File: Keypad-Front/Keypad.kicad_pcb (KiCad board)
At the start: 4 copper layers, 100.1 x 192.1 mm, 62 parts, among them J1 RTC STEMMA QT, J3 JST-PH 6, J4 JST-PH 6, J6 EXP QWIIC, J7 TOUCH QWIIC, U1 DS3231MZ, U2 LM1117-3.3, U3 CAP1214

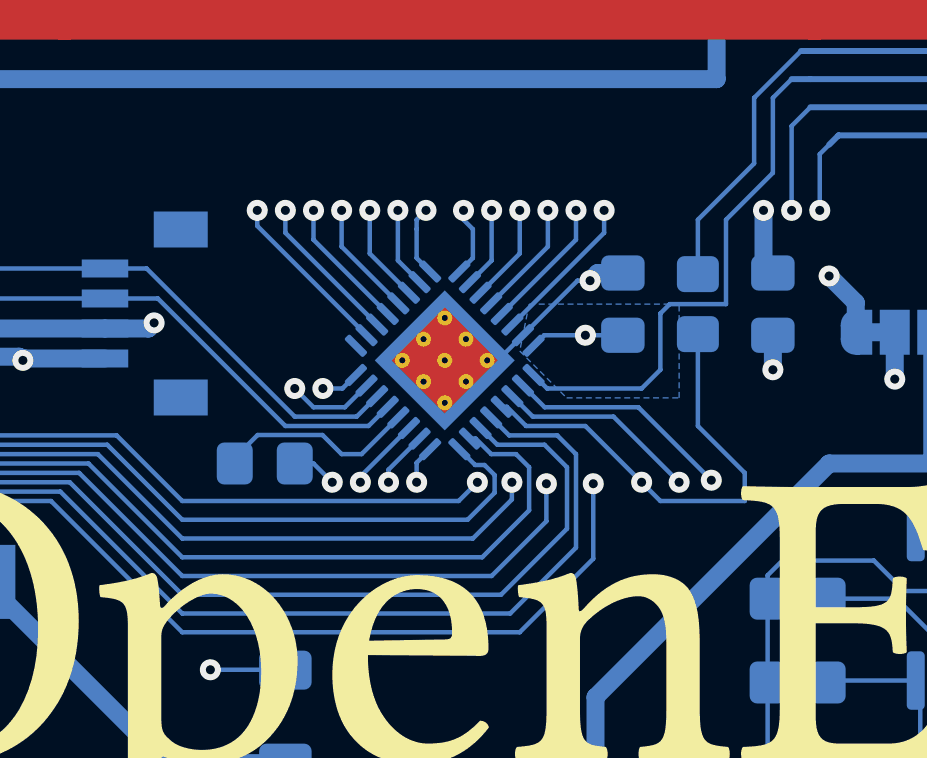
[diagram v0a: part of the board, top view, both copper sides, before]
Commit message: Fix schematic and PCB
1. Swap LED6 and LED11 so that the dual LED is on the high-power port.
   (This change isn't green-wired on the existing boards.)
2. Add 47pF series cap to TOUCH_GUARD to bring it into spec.
   (Measured at 80pF; CAP1214 supports 50pF max.)
3. Fix RESET -- it should be grounded, not tied high.
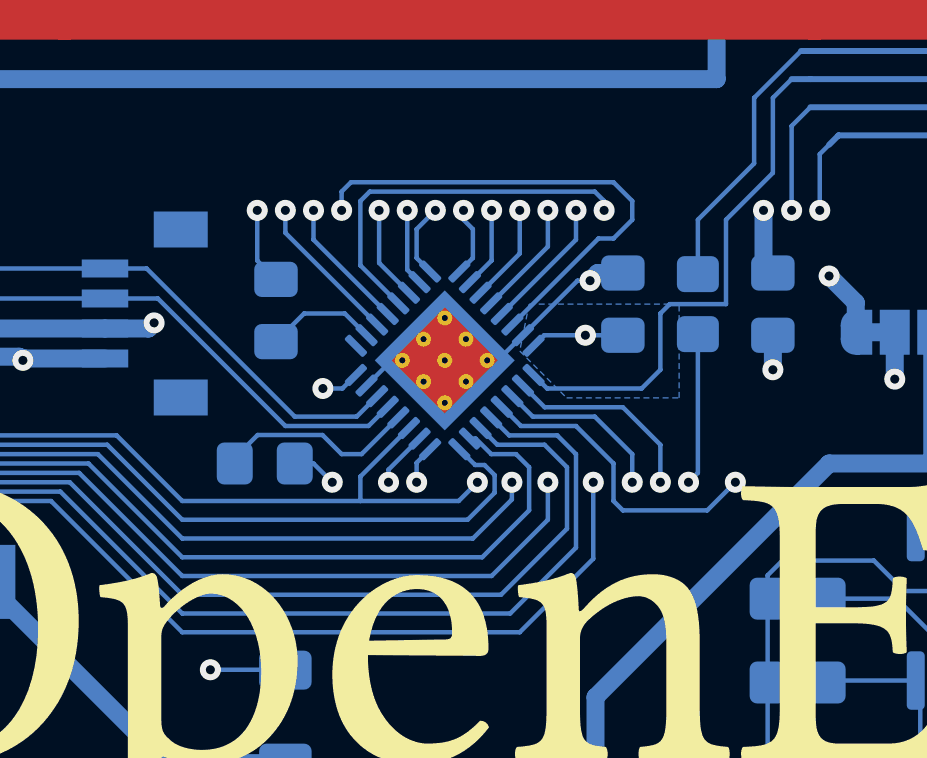
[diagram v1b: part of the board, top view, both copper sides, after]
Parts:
- added C5: 47pF, Capacitor_SMD:C_0805_2012Metric_Pad1.18x1.45mm_HandSolder, B.Cu at (102.5, 185.2)
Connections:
- U3 pad 12: /LED10 -> /LED6
- U3 pad 19: /LED6 -> /LED10
- U3 pad 23: +3.3V -> GND1
- U3 pad 26: /TOUCH_GUARD -> Net-(U3-CS1)
- U3 pad 29: /TOUCH_10 -> /TOUCH_6
- U3 pad 6: /TOUCH_6 -> /TOUCH_10
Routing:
- net /TOUCH_10: track 35.9 -> 48.8 mm
- net /TOUCH_5: track 77.5 -> 69.7 mm
- net /TOUCH_6: track 102.8 -> 110.3 mm
- net /LED10: track 89.2 -> 83.2 mm
- net /TOUCH_1: track 107.8 -> 101.9 mm
- net /LED6: track 134.4 -> 129.6 mm
- net +3.3V: track 58.3 -> 54.3 mm, vias 6 -> 5
- net /LED7: track 112.3 -> 108.6 mm
- net Net-(U3-CS1): track 0.00 -> 3.71 mm
- net /TOUCH_8: track 50.4 -> 46.8 mm
- net /LED4: track 144.2 -> 140.6 mm
- net /LED3: track 157.8 -> 161.2 mm
- net /TOUCH_GUARD: track 41.6 -> 38.5 mm
- net GND1: track 2021.0 -> 2022.5 mm

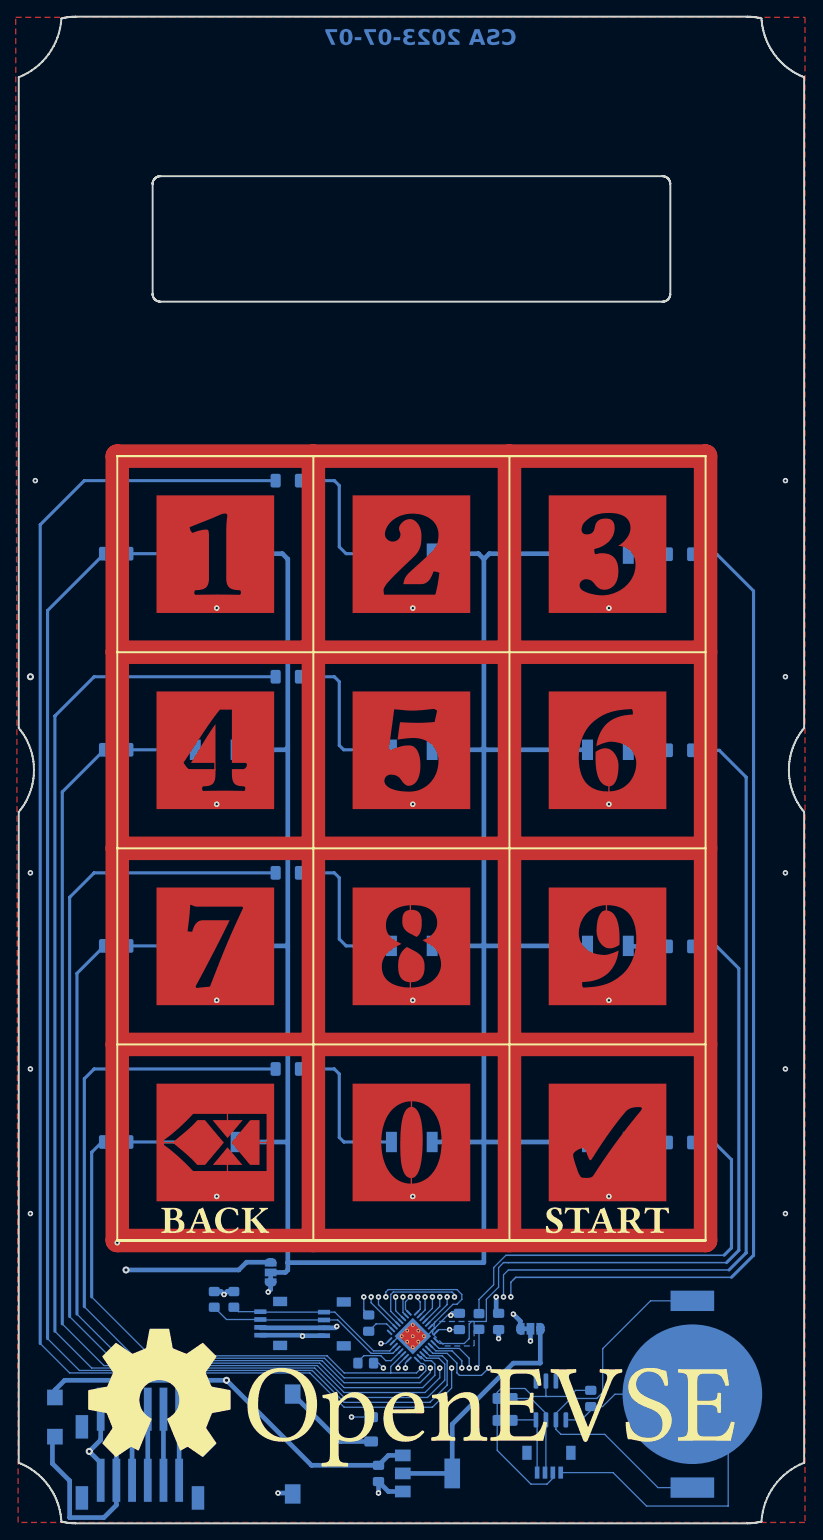
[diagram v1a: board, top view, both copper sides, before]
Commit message: Fix some errors in original boards; add RFID functionality
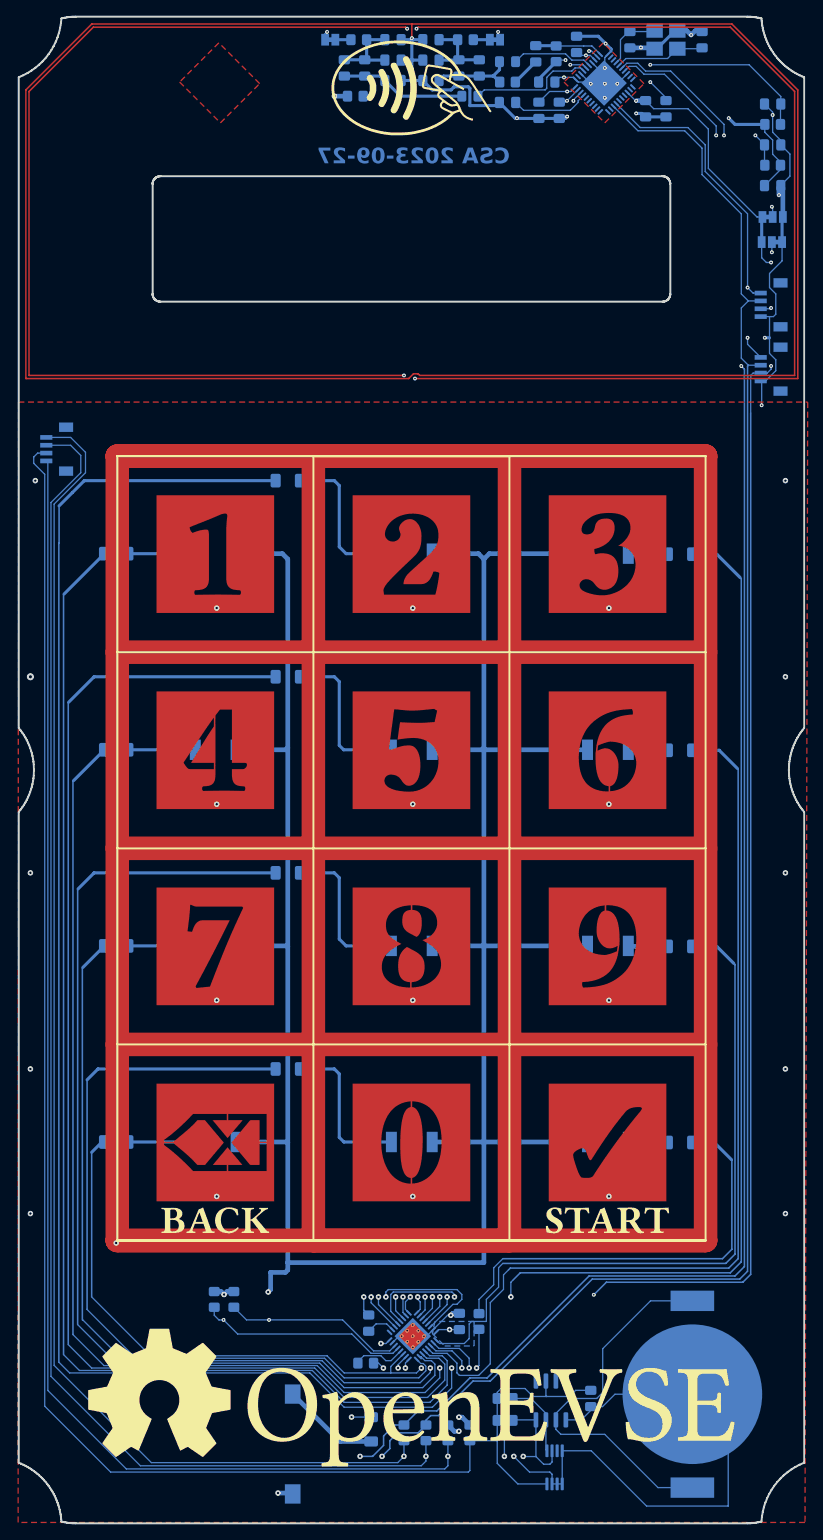
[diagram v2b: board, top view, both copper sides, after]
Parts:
- removed J3, J4: JST-PH 6, Keypad:JST-PH-6-SMD
- removed TP13: 5V, TestPoint:TestPoint_Pad_2.0x2.0mm
- removed TP14: Guard, Keypad:Touch_Pad_D1.0mm
- removed TP15: 12V, TestPoint:TestPoint_Pad_2.0x2.0mm
- removed U2: LM1117-3.3, Package_TO_SOT_SMD:SOT-223-3_TabPin2
- added C10: 10uF, Capacitor_SMD:C_0805_2012Metric_Pad1.18x1.45mm_HandSolder, B.Cu at (154.0, 29.8)
- added C11: .1uF, Capacitor_SMD:C_0805_2012Metric_Pad1.18x1.45mm_HandSolder, B.Cu at (129.0, 22.2)
- added C12: N/C, Capacitor_SMD:C_0805_2012Metric_Pad1.18x1.45mm_HandSolder, B.Cu at (99.4, 25.2)
- added C13: .1uF, Capacitor_SMD:C_0805_2012Metric_Pad1.18x1.45mm_HandSolder, B.Cu at (154.0, 40.2)
- added C14: 10uF, Capacitor_SMD:C_0805_2012Metric_Pad1.18x1.45mm_HandSolder, B.Cu at (154.0, 35.0)
- added C15: .1uF, Capacitor_SMD:C_0805_2012Metric_Pad1.18x1.45mm_HandSolder, B.Cu at (140.4, 30.4)
- added C16: 220pF, Capacitor_SMD:C_0805_2012Metric_Pad1.18x1.45mm_HandSolder, B.Cu at (105.6, 26.8)
- added C17: 220pF, Capacitor_SMD:C_0805_2012Metric_Pad1.18x1.45mm_HandSolder, B.Cu at (110.4, 26.8)
- added C18: N/C, Capacitor_SMD:C_0805_2012Metric_Pad1.18x1.45mm_HandSolder, B.Cu at (116.6, 25.2)
- added C19: 22pF, Capacitor_SMD:C_0805_2012Metric_Pad1.18x1.45mm_HandSolder, B.Cu at (102.0, 25.2)
- added C20: 22pF, Capacitor_SMD:C_0805_2012Metric_Pad1.18x1.45mm_HandSolder, B.Cu at (114.0, 25.2)
- added C21: 100pF, Capacitor_SMD:C_0805_2012Metric_Pad1.18x1.45mm_HandSolder, B.Cu at (105.6, 24.2)
- added C22: 100pF, Capacitor_SMD:C_0805_2012Metric_Pad1.18x1.45mm_HandSolder, B.Cu at (110.4, 24.2)
- added C23: N/C, Capacitor_SMD:C_0805_2012Metric_Pad1.18x1.45mm_HandSolder, B.Cu at (105.6, 21.6)
- added C24: N/C, Capacitor_SMD:C_0805_2012Metric_Pad1.18x1.45mm_HandSolder, B.Cu at (110.4, 21.6)
- added C25: 1000pF, Capacitor_SMD:C_0805_2012Metric_Pad1.18x1.45mm_HandSolder, B.Cu at (123.8, 23.4)
- added C26: .1uF, Capacitor_SMD:C_0805_2012Metric_Pad1.18x1.45mm_HandSolder, B.Cu at (125.2, 27.0)
- added C6: .1uF, Capacitor_SMD:C_0805_2012Metric_Pad1.18x1.45mm_HandSolder, B.Cu at (137.8, 30.4)
- added C7: .1uF, Capacitor_SMD:C_0805_2012Metric_Pad1.18x1.45mm_HandSolder, B.Cu at (126.8, 30.6)
- added C8: .1uF, Capacitor_SMD:C_0805_2012Metric_Pad1.18x1.45mm_HandSolder, B.Cu at (124.2, 30.6)
- added C9: 10uF, Capacitor_SMD:C_0805_2012Metric_Pad1.18x1.45mm_HandSolder, B.Cu at (120.2, 29.6)
- added FB1: FerriteBead_Small, Resistor_SMD:R_0805_2012Metric_Pad1.20x1.40mm_HandSolder, B.Cu at (154.0, 32.4)
- added FB2: FerriteBead_Small, Resistor_SMD:R_0805_2012Metric_Pad1.20x1.40mm_HandSolder, B.Cu at (154.0, 37.6)
- added L1: 560nH, Inductor_SMD:L_0805_2012Metric_Pad1.15x1.40mm_HandSolder, B.Cu at (115.4, 28.8)
- added L2: 560nH, Inductor_SMD:L_0805_2012Metric_Pad1.15x1.40mm_HandSolder, B.Cu at (120.2, 24.4)
- added R20: 10k, Resistor_SMD:R_0805_2012Metric_Pad1.20x1.40mm_HandSolder, B.Cu at (100.8, 28.8)
- added R21: 1.5, Resistor_SMD:R_0805_2012Metric_Pad1.20x1.40mm_HandSolder, B.Cu at (101.2, 21.6)
- added R22: 1.5, Resistor_SMD:R_0805_2012Metric_Pad1.20x1.40mm_HandSolder, B.Cu at (114.8, 21.6)
- added R23: N/C, Jumper:SolderJumper-2_P1.3mm_Bridged_Pad1.0x1.5mm, B.Cu at (97.6, 21.6)
- added R24: N/C, Jumper:SolderJumper-2_P1.3mm_Bridged_Pad1.0x1.5mm, B.Cu at (118.6, 21.6)
- added R25: 2.7k, Resistor_SMD:R_0805_2012Metric_Pad1.20x1.40mm_HandSolder, B.Cu at (120.2, 27.0)
- added R26: 1.0k, Resistor_SMD:R_0805_2012Metric_Pad1.20x1.40mm_HandSolder, B.Cu at (126.4, 23.4)
- added R27: 0, Resistor_SMD:R_0805_2012Metric_Pad1.20x1.40mm_HandSolder, B.Cu at (107.0, 199.2)
- added R28: 0, Resistor_SMD:R_0805_2012Metric_Pad1.20x1.40mm_HandSolder, B.Cu at (109.8, 199.2)
- added R29: 0, Resistor_SMD:R_0805_2012Metric_Pad1.20x1.40mm_HandSolder, B.Cu at (115.4, 199.2)
- added R30: 0, Resistor_SMD:R_0805_2012Metric_Pad1.20x1.40mm_HandSolder, B.Cu at (112.6, 199.2)
- added U4: PN5321A3HN_C1xx, Package_DFN_QFN:HVQFN-40-1EP_6x6mm_P0.5mm_EP4.1x4.1mm, B.Cu at (132.5, 27.1)
- added U5: MCP9808_MSOP, Package_SO:MSOP-8_3x3mm_P0.65mm, B.Cu at (126.2, 203.6)
- added Y3: 27.12MHz, Crystal:Crystal_SMD_TXC_7M-4Pin_3.2x2.5mm_HandSoldering, B.Cu at (140.4, 21.6)
- C2, C3: value 10uF -> 33pF
- JP1: value PWR SEL -> SEL0; footprint Jumper:SolderJumper-3_P1.3mm_Bridged12_RoundedPad1.0x1.5mm -> Jumper:SolderJumper-3_P1.3mm_Bridged12_Pad1.0x1.5mm
- JP2: value PWR SEL -> SEL1; footprint Jumper:SolderJumper-3_P1.3mm_Bridged12_RoundedPad1.0x1.5mm -> Jumper:SolderJumper-3_P1.3mm_Bridged12_Pad1.0x1.5mm
- moved C3 187.4 mm to (145.0, 21.6)
- moved C2 164.3 mm to (135.8, 21.6)
- moved JP2 149.0 mm to (154.0, 44.2), turned to 0 degrees
- moved J1 145.4 mm to (61.4, 73.8), turned to -90 degrees
- moved J7 144.7 mm to (152.5, 55.4)
- moved JP1 141.9 mm to (153.9, 47.4), turned to 180 degrees
- moved J6 133.8 mm to (152.5, 63.6)
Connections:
- C2 pad 1: +3.3V -> GND1
- C2 pad 2: GND1 -> Net-(U4-OSCIN)
- C3 pad 1: /DC_IN -> GND1
- C3 pad 2: GND1 -> Net-(U4-OSCOUT)
- D1 pad 2: /LED_VIN -> +3.3V
- D10 pad 2: /LED_VIN -> +3.3V
- D11 pad 2: /LED_VIN -> +3.3V
- D12 pad 2: /LED_VIN -> +3.3V
- D2 pad 2: /LED_VIN -> +3.3V
- D3 pad 2: /LED_VIN -> +3.3V
- D4 pad 2: /LED_VIN -> +3.3V
- D5 pad 2: /LED_VIN -> +3.3V
- D6 pad 2: /LED_VIN -> +3.3V
- D7 pad 2: /LED_VIN -> +3.3V
- D8 pad 2: /LED_VIN -> +3.3V
- D9 pad 2: /LED_VIN -> +3.3V
- J6 pad 2: /TOUCH_VIN -> +3.3V
- J7 pad 2: /TOUCH_VIN -> +3.3V
- JP1 pad 1: /TOUCH_VIN -> GND1
- JP1 pad 2: +3.3V -> /SEL1
- JP1 pad 3: /VREG -> +3.3V
- JP2 pad 2: /LED_VIN -> /SEL0
- JP2 pad 3: /DC_IN -> GND1
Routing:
- net GND1: track 2022.5 -> 2623.3 mm, vias 17 -> 39
- net +3.3V: track 54.3 -> 635.9 mm, vias 5 -> 11
- net /LED_VIN: track 314.5 -> 0.00 mm
- net /TOUCH_SDA: track 26.1 -> 277.7 mm, vias 0 -> 2
- net /TOUCH_SCL: track 23.1 -> 269.5 mm, vias 0 -> 5
- net GND2: track 57.0 -> 256.7 mm, vias 0 -> 2
- net /RTC_SCL: track 9.75 -> 205.4 mm, vias 0 -> 2
- net /RTC_SDA: track 12.6 -> 207.4 mm, vias 0 -> 2
- net +5V: track 32.3 -> 219.9 mm
- net /DC_IN: track 104.1 -> 0.00 mm, vias 2 -> 0
- net VCC: track 0.00 -> 39.5 mm, vias 0 -> 2
- net Net-(U4-TVDD): track 0.00 -> 38.2 mm, vias 0 -> 3
- net /SEL1: track 0.00 -> 37.3 mm, vias 0 -> 2
- net /TOUCH_VIN: track 36.0 -> 0.00 mm, vias 2 -> 0
- net Net-(U4-AVDD): track 0.00 -> 34.3 mm, vias 0 -> 2
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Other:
- board text added: "0"
- board text added: "1"
- board text added: "CSA 2023-09-27"
- board text added: "ESP32 QWIIC"
- board text added: "LCD QWIIC"
- board text added: "OpenEVSE Keypad+RFID Add-On C. Scott Ananian"
- board text added: "Opt. I2C BRIDGE"
- board text removed: "+12V"
- board text removed: "+3.3V"
- board text removed: "+5V"
- board text removed: "CSA 2023-07-07"
- board text removed: "LED SUPPLY"
- board text removed: "OPT REG"
- board text removed: "OpenEVSE Keypad Add-On C. Scott Ananian"
- board text removed: "Optional Power Tap"
- board text removed: "RTC I2C"
- board text removed: "STEMMA QT"

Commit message: Relocate traces for keypad 2/5/8 which got moved somehow
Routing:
- net /TOUCH_5: track 69.7 -> 76.9 mm
- net /TOUCH_1: track 101.9 -> 107.8 mm
- net /TOUCH_8: track 44.3 -> 50.0 mm
- net /TOUCH_11: track 19.0 -> 17.0 mm
- net /TOUCH_2: track 102.0 -> 101.1 mm

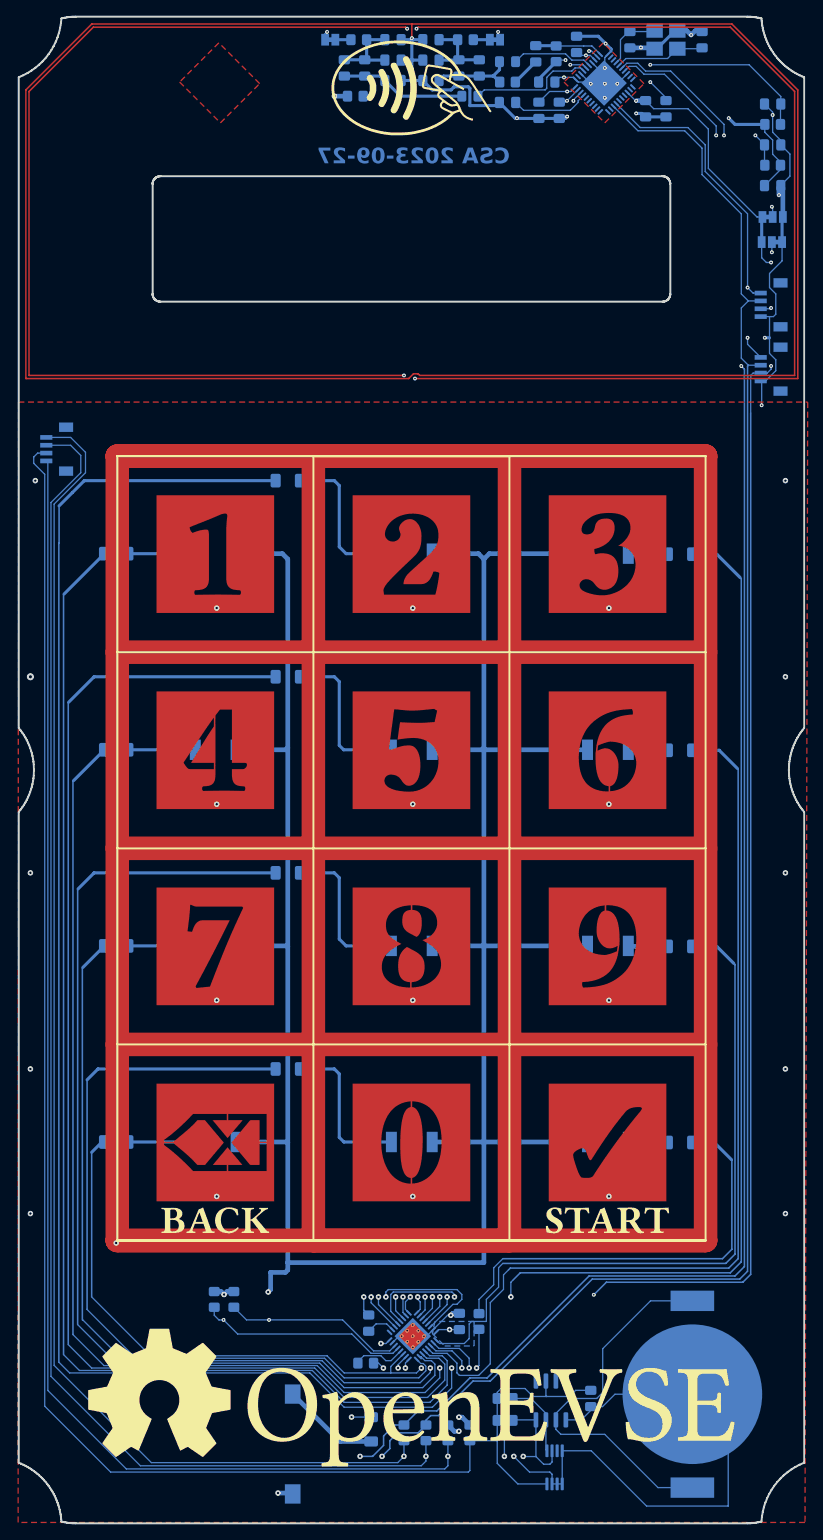
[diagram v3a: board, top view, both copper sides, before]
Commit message: Add PCA9536 I/O expander to handle LED12 and hardware version detect
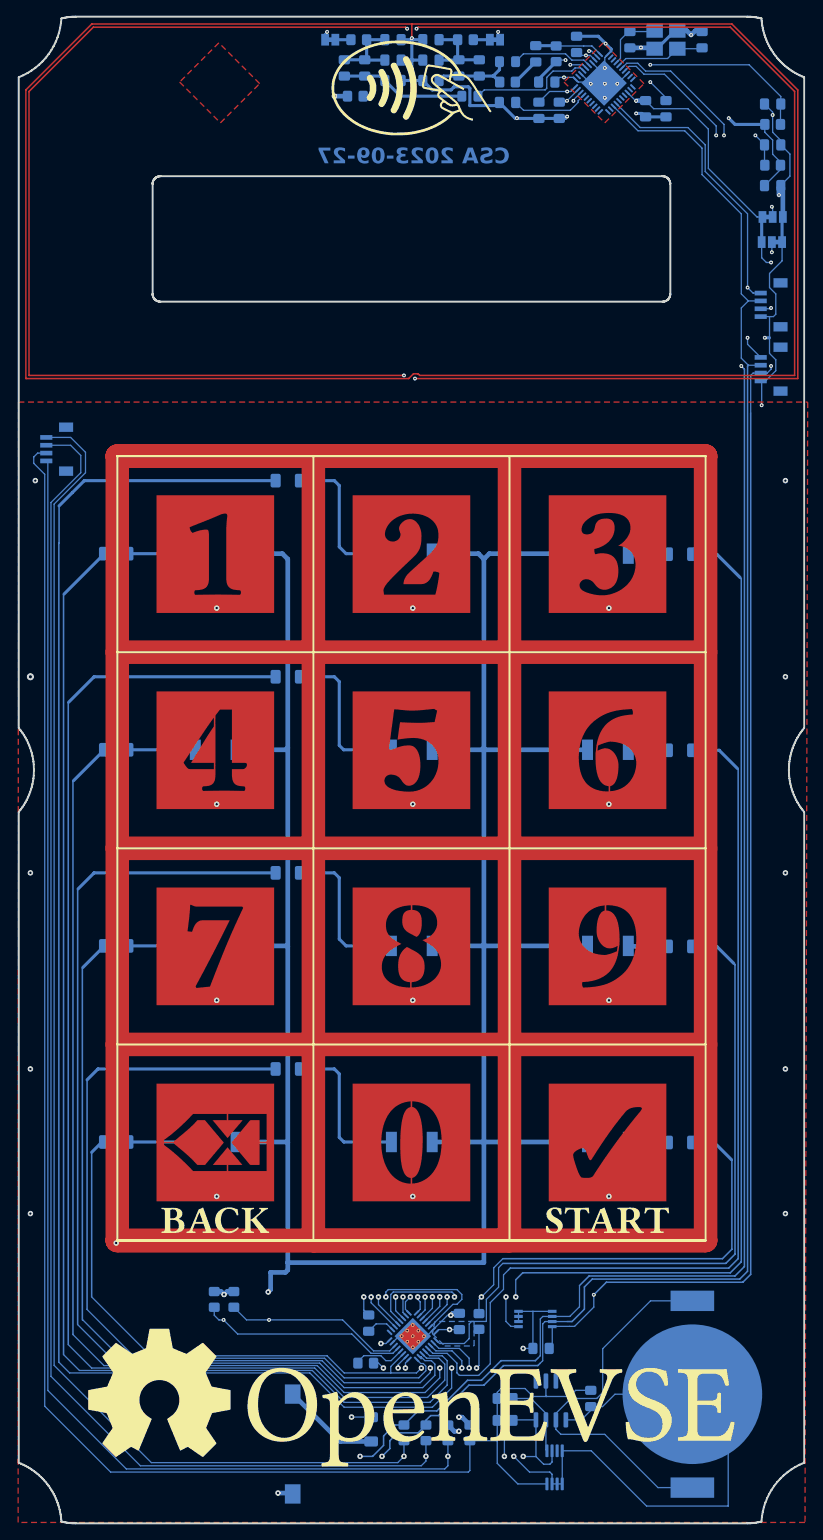
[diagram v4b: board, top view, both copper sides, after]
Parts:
- added C27: .1uF, Capacitor_SMD:C_0805_2012Metric_Pad1.18x1.45mm_HandSolder, B.Cu at (124.5, 188.4)
- added TP14: Guard, Keypad:Touch_Pad_D1.0mm, F.Cu at (70.3, 173.1)
- added U2: PCA9536DP, Package_SO:TSSOP-8_3x3mm_P0.65mm, B.Cu at (123.8, 184.7)
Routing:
- net GND1: track 2623.3 -> 2636.9 mm, vias 39 -> 40
- net +3.3V: track 635.9 -> 647.7 mm
- net /LED12: track 55.3 -> 63.4 mm, vias 0 -> 2
- net /TOUCH_SDA: track 277.7 -> 282.1 mm
- net /TOUCH_SCL: track 269.5 -> 273.8 mm
- net /TOUCH_GUARD: track 37.0 -> 38.8 mm
